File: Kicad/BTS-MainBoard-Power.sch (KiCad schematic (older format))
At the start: 46 parts, among them J1 +12VIn, J10 Conn_01x02, J11 Conn_01x02, J12 Conn_01x02, J13 Conn_01x02, J14 Conn_01x02, J15 Conn_01x02, J16 Conn_01x02, J17 Conn_01x02, J18 Conn_01x02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

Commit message: Renamed Libraries and renamed project files as well
Signed-off-by: bebenlebricolo <benoittarrade@hotmail.fr>
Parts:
- removed U2, U3, U4, U5: STD80N6F6, Package_TO_SOT_SMD:TO-252-2, symbol STD80N6F6:STD80N6F6
- added Q1, Q2, Q3, Q4: STD80N6F6, Package_TO_SOT_SMD:TO-252-2, symbol Device:Q_NMOS_GDS
- J1, J2: footprint PeltierSwitchingMainBoard:Power_Solder_Pad_7x15mm -> BTS-MainBoard-Power:Power_Solder_Pad_7x15mm
- J10, J11, J4, J5, J6, J7, J8, J9: footprint PeltierSwitchingMainBoard:Power_Solder_Pad_5x10mm_02 -> BTS-MainBoard-Power:Power_Solder_Pad_5x10mm_02
- L1, L2, L3, L4: footprint PeltierSwitchingMainBoard:L_Bourns_SRP1270 -> BTS-MainBoard-Power:L_Bourns_SRP1270
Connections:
- net +12V: now also Q1.2 (D), Q3.2 (D)
- net AHS: now also Q1.3 (S), Q2.2 (D)
- net ALS: now also Q2.3 (S), Q4.3 (S)
- net BHS: now also Q3.3 (S), Q4.2 (D)
- net at R8.1: now also Q2.1 (G)
- net at R7.1: now also Q1.1 (G)
- net at R10.1: now also Q3.1 (G)
- net at R11.1: now also Q4.1 (G)
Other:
- moved on the sheet: R10, R11, R7, R8
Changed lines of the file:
@@
 $EndDescr
-$Comp
-L STD80N6F6:STD80N6F6 U3
-U 1 1 6138C674
-P 5900 3900
-F 0 "U3" H 6330 4053 60  0000 L CNN
-F 1 "STD80N6F6" H 6330 3947 60  0000 L CNN
-F 2 "Package_TO_SOT_SMD:TO-252-2" H 6350 3740 60  0001 C CNN
-F 3 "" H 5900 3900 60  0000 C CNN
-	1    5900 3900
-	1    0    0    -1
-$EndComp
 $Comp
 L power:+12V #PWR01
@@
 L Device:R R7
 U 1 1 613B719E
-P 5750 2650
-F 0 "R7" V 5543 2650 50  0000 C CNN
-F 1 "3.3" V 5634 2650 50  0000 C CNN
-F 2 "Resistor_SMD:R_1206_3216Metric_Pad1.30x1.75mm_HandSolder" V 5680 2650 50  0001 C CNN
-F 3 "~" H 5750 2650 50  0001 C CNN
-	1    5750 2650
+P 5750 2600
+F 0 "R7" V 5543 2600 50  0000 C CNN
+F 1 "3.3" V 5634 2600 50  0000 C CNN
+F 2 "Resistor_SMD:R_1206_3216Metric_Pad1.30x1.75mm_HandSolder" V 5680 2600 50  0001 C CNN
+F 3 "~" H 5750 2600 50  0001 C CNN
+	1    5750 2600
 	0    1    1    0
 $EndComp
@@
 L Device:R R8
 U 1 1 613BA065
-P 5750 3900
-F 0 "R8" V 5543 3900 50  0000 C CNN
-F 1 "3.3" V 5634 3900 50  0000 C CNN
-F 2 "Resistor_SMD:R_1206_3216Metric_Pad1.30x1.75mm_HandSolder" V 5680 3900 50  0001 C CNN
-F 3 "~" H 5750 3900 50  0001 C CNN
-	1    5750 3900
+P 5750 3850
+F 0 "R8" V 5543 3850 50  0000 C CNN
+F 1 "3.3" V 5634 3850 50  0000 C CNN
+F 2 "Resistor_SMD:R_1206_3216Metric_Pad1.30x1.75mm_HandSolder" V 5680 3850 50  0001 C CNN
+F 3 "~" H 5750 3850 50  0001 C CNN
+	1    5750 3850
 	0    1    1    0
 $EndComp
@@
 L Device:R R10
 U 1 1 613C9CA0
-P 7250 2650
-F 0 "R10" V 7043 2650 50  0000 C CNN
-F 1 "3.3" V 7134 2650 50  0000 C CNN
-F 2 "Resistor_SMD:R_1206_3216Metric_Pad1.30x1.75mm_HandSolder" V 7180 2650 50  0001 C CNN
-F 3 "~" H 7250 2650 50  0001 C CNN
-	1    7250 2650
+P 7250 2600
+F 0 "R10" V 7043 2600 50  0000 C CNN
+F 1 "3.3" V 7134 2600 50  0000 C CNN
+F 2 "Resistor_SMD:R_1206_3216Metric_Pad1.30x1.75mm_HandSolder" V 7180 2600 50  0001 C CNN
+F 3 "~" H 7250 2600 50  0001 C CNN
+	1    7250 2600
 	0    1    1    0
 $EndComp
@@
 L Device:R R11
 U 1 1 613CB9E6
-P 7250 3900
-F 0 "R11" V 7043 3900 50  0000 C CNN
-F 1 "3.3" V 7134 3900 50  0000 C CNN
-F 2 "Resistor_SMD:R_1206_3216Metric_Pad1.30x1.75mm_HandSolder" V 7180 3900 50  0001 C CNN
-F 3 "~" H 7250 3900 50  0001 C CNN
-	1    7250 3900
+P 7250 3850
+F 0 "R11" V 7043 3850 50  0000 C CNN
+F 1 "3.3" V 7134 3850 50  0000 C CNN
+F 2 "Resistor_SMD:R_1206_3216Metric_Pad1.30x1.75mm_HandSolder" V 7180 3850 50  0001 C CNN
+F 3 "~" H 7250 3850 50  0001 C CNN
+	1    7250 3850
 	0    1    1    0
 $EndComp
@@
 Wire Wire Line
 	6950 4500 7700 4500
-$Comp
-L STD80N6F6:STD80N6F6 U2
-U 1 1 613DD883
-P 5900 2650
-F 0 "U2" H 6330 2803 60  0000 L CNN
-F 1 "STD80N6F6" H 6330 2697 60  0000 L CNN
-F 2 "Package_TO_SOT_SMD:TO-252-2" H 6350 2490 60  0001 C CNN
-F 3 "" H 5900 2650 60  0000 C CNN
-	1    5900 2650
-	1    0    0    -1
-$EndComp
-$Comp
-L STD80N6F6:STD80N6F6 U5
-U 1 1 613DED8D
-P 7400 3900
-F 0 "U5" H 7830 4053 60  0000 L CNN
-F 1 "STD80N6F6" H 7830 3947 60  0000 L CNN
-F 2 "Package_TO_SOT_SMD:TO-252-2" H 7850 3740 60  0001 C CNN
-F 3 "" H 7400 3900 60  0000 C CNN
-	1    7400 3900
-	1    0    0    -1
-$EndComp
-Text Label 5600 3900 2    50   ~ 0
+Text Label 5600 3850 2    50   ~ 0
 ALO
-Text Label 7100 2650 2    50   ~ 0
+Text Label 7100 2600 2    50   ~ 0
 BHO
-Text Label 7100 3900 2    50   ~ 0
+Text Label 7100 3850 2    50   ~ 0
 BLO
 Wire Wire Line
@@
 F 0 "L3" V 6790 3400 50  0000 C CNN
 F 1 "SRP1270-100M" V 6699 3400 50  0000 C CNN
-F 2 "PeltierSwitchingMainBoard:L_Bourns_SRP1270" H 6600 3400 50  0001 C CNN
+F 2 "BTS-MainBoard-Power:L_Bourns_SRP1270" H 6600 3400 50  0001 C CNN
 F 3 "~" H 6600 3400 50  0001 C CNN
 	1    6600 3400
@@
 F 0 "L4" V 6790 3650 50  0000 C CNN
 F 1 "SRP1270-100M" V 6699 3650 50  0000 C CNN
-F 2 "PeltierSwitchingMainBoard:L_Bourns_SRP1270" H 6600 3650 50  0001 C CNN
+F 2 "BTS-MainBoard-Power:L_Bourns_SRP1270" H 6600 3650 50  0001 C CNN
 F 3 "~" H 6600 3650 50  0001 C CNN
 	1    6600 3650
@@
 F 0 "L1" V 6790 2900 50  0000 C CNN
 F 1 "SRP1270-100M" V 6699 2900 50  0000 C CNN
-F 2 "PeltierSwitchingMainBoard:L_Bourns_SRP1270" H 6600 2900 50  0001 C CNN
+F 2 "BTS-MainBoard-Power:L_Bourns_SRP1270" H 6600 2900 50  0001 C CNN
 F 3 "~" H 6600 2900 50  0001 C CNN
 	1    6600 2900
@@
 F 0 "L2" V 6790 3200 50  0000 C CNN
 F 1 "SRP1270-100M" V 6699 3200 50  0000 C CNN
-F 2 "PeltierSwitchingMainBoard:L_Bourns_SRP1270" H 6600 3200 50  0001 C CNN
+F 2 "BTS-MainBoard-Power:L_Bourns_SRP1270" H 6600 3200 50  0001 C CNN
 F 3 "~" H 6600 3200 50  0001 C CNN
 	1    6600 3200
@@
 Wire Wire Line
 	7700 2800 7700 2950
-Wire Wire Line
-	7700 1650 7700 2300
-$Comp
-L STD80N6F6:STD80N6F6 U4
-U 1 1 613DE25E
-P 7400 2650
-F 0 "U4" H 7830 2803 60  0000 L CNN
-F 1 "STD80N6F6" H 7830 2697 60  0000 L CNN
-F 2 "Package_TO_SOT_SMD:TO-252-2" H 7850 2490 60  0001 C CNN
-F 3 "" H 7400 2650 60  0000 C CNN
-	1    7400 2650
-	1    0    0    -1
-$EndComp
-Wire Wire Line
-	6200 2300 6200 1650
-Wire Wire Line
-	7700 3550 7700 3200
 Connection ~ 7700 3200
 Wire Wire Line
@@
 	6200 4050 6200 4300
 Connection ~ 6200 4300
-Wire Wire Line
-	6200 3550 6200 3250
 Connection ~ 6200 3250
 $Comp
@@
 F 0 "J1" H 4330 1142 50  0000 L CNN
 F 1 "+12VIn" H 4330 1051 50  0000 L CNN
-F 2 "PeltierSwitchingMainBoard:Power_Solder_Pad_7x15mm" H 4250 1100 50  0001 C CNN
+F 2 "BTS-MainBoard-Power:Power_Solder_Pad_7x15mm" H 4250 1100 50  0001 C CNN
 F 3 "~" H 4250 1100 50  0001 C CNN
 	1    4250 1100
@@
 F 0 "J2" H 4330 1342 50  0000 L CNN
 F 1 "GNDIn" H 4330 1251 50  0000 L CNN
-F 2 "PeltierSwitchingMainBoard:Power_Solder_Pad_7x15mm" H 4250 1300 50  0001 C CNN
+F 2 "BTS-MainBoard-Power:Power_Solder_Pad_7x15mm" H 4250 1300 50  0001 C CNN
 F 3 "~" H 4250 1300 50  0001 C CNN
 	1    4250 1300
@@
 F 0 "J4" H 10130 1092 50  0000 L CNN
 F 1 "Conn_01x02" H 10130 1001 50  0000 L CNN
-F 2 "PeltierSwitchingMainBoard:Power_Solder_Pad_5x10mm_02" H 10050 1100 50  0001 C CNN
+F 2 "BTS-MainBoard-Power:Power_Solder_Pad_5x10mm_02" H 10050 1100 50  0001 C CNN
 F 3 "~" H 10050 1100 50  0001 C CNN
 	1    10050 1100
@@
 F 0 "J5" H 10130 1342 50  0000 L CNN
 F 1 "Conn_01x02" H 10130 1251 50  0000 L CNN
-F 2 "PeltierSwitchingMainBoard:Power_Solder_Pad_5x10mm_02" H 10050 1350 50  0001 C CNN
+F 2 "BTS-MainBoard-Power:Power_Solder_Pad_5x10mm_02" H 10050 1350 50  0001 C CNN
 F 3 "~" H 10050 1350 50  0001 C CNN
 	1    10050 1350
@@
 F 0 "J6" H 10130 1592 50  0000 L CNN
 F 1 "Conn_01x02" H 10130 1501 50  0000 L CNN
-F 2 "PeltierSwitchingMainBoard:Power_Solder_Pad_5x10mm_02" H 10050 1600 50  0001 C CNN
+F 2 "BTS-MainBoard-Power:Power_Solder_Pad_5x10mm_02" H 10050 1600 50  0001 C CNN
 F 3 "~" H 10050 1600 50  0001 C CNN
 	1    10050 1600
@@
 F 0 "J7" H 10130 1842 50  0000 L CNN
 F 1 "Conn_01x02" H 10130 1751 50  0000 L CNN
-F 2 "PeltierSwitchingMainBoard:Power_Solder_Pad_5x10mm_02" H 10050 1850 50  0001 C CNN
+F 2 "BTS-MainBoard-Power:Power_Solder_Pad_5x10mm_02" H 10050 1850 50  0001 C CNN
 F 3 "~" H 10050 1850 50  0001 C CNN
 	1    10050 1850
@@
 F 0 "J8" H 10130 2092 50  0000 L CNN
 F 1 "Conn_01x02" H 10130 2001 50  0000 L CNN
-F 2 "PeltierSwitchingMainBoard:Power_Solder_Pad_5x10mm_02" H 10050 2100 50  0001 C CNN
+F 2 "BTS-MainBoard-Power:Power_Solder_Pad_5x10mm_02" H 10050 2100 50  0001 C CNN
 F 3 "~" H 10050 2100 50  0001 C CNN
 	1    10050 2100
@@
 F 0 "J9" H 10130 2342 50  0000 L CNN
 F 1 "Conn_01x02" H 10130 2251 50  0000 L CNN
-F 2 "PeltierSwitchingMainBoard:Power_Solder_Pad_5x10mm_02" H 10050 2350 50  0001 C CNN
+F 2 "BTS-MainBoard-Power:Power_Solder_Pad_5x10mm_02" H 10050 2350 50  0001 C CNN
 F 3 "~" H 10050 2350 50  0001 C CNN
 	1    10050 2350
@@
 F 0 "J10" H 10130 2592 50  0000 L CNN
 F 1 "Conn_01x02" H 10130 2501 50  0000 L CNN
-F 2 "PeltierSwitchingMainBoard:Power_Solder_Pad_5x10mm_02" H 10050 2600 50  0001 C CNN
+F 2 "BTS-MainBoard-Power:Power_Solder_Pad_5x10mm_02" H 10050 2600 50  0001 C CNN
 F 3 "~" H 10050 2600 50  0001 C CNN
 	1    10050 2600
@@
 F 0 "J11" H 10130 2842 50  0000 L CNN
 F 1 "Conn_01x02" H 10130 2751 50  0000 L CNN
-F 2 "PeltierSwitchingMainBoard:Power_Solder_Pad_5x10mm_02" H 10050 2850 50  0001 C CNN
+F 2 "BTS-MainBoard-Power:Power_Solder_Pad_5x10mm_02" H 10050 2850 50  0001 C CNN
 F 3 "~" H 10050 2850 50  0001 C CNN
 	1    10050 2850
@@
 	0    1    1    0
 $EndComp
-Text Label 5600 2650 2    50   ~ 0
+Text Label 5600 2600 2    50   ~ 0
 AHO
 Wire Wire Line
@@
 Text Notes 9800 6450 0    50   Italic 0
 Designed by Benoit Tarrade\n(alias bebenlebricolo)\nhttps://github.com/bebenlebricolo
+$Comp
+L Device:Q_NMOS_GDS Q1
+U 1 1 6140C534
+P 6100 2600
+F 0 "Q1" H 6305 2646 50  0000 L CNN
+F 1 "STD80N6F6" H 6305 2555 50  0000 L CNN
+F 2 "Package_TO_SOT_SMD:TO-252-2" H 6300 2700 50  0001 C CNN
+F 3 "~" H 6100 2600 50  0001 C CNN
+	1    6100 2600
+	1    0    0    -1
+$EndComp
+Wire Wire Line
+	6200 3250 6200 3650
+Wire Wire Line
+	6200 1650 6200 2400
+Wire Wire Line
+	7700 3200 7700 3650
+Wire Wire Line
+	7700 1650 7700 2400
+$Comp
+L Device:Q_NMOS_GDS Q3
+U 1 1 61418DBA
+P 7600 2600
+F 0 "Q3" H 7805 2646 50  0000 L CNN
+F 1 "STD80N6F6" H 7805 2555 50  0000 L CNN
+F 2 "Package_TO_SOT_SMD:TO-252-2" H 7800 2700 50  0001 C CNN
+F 3 "~" H 7600 2600 50  0001 C CNN
+	1    7600 2600
+	1    0    0    -1
+$EndComp
+$Comp
+L Device:Q_NMOS_GDS Q4
+U 1 1 614197F7
+P 7600 3850
+F 0 "Q4" H 7805 3896 50  0000 L CNN
+F 1 "STD80N6F6" H 7805 3805 50  0000 L CNN
+F 2 "Package_TO_SOT_SMD:TO-252-2" H 7800 3950 50  0001 C CNN
+F 3 "~" H 7600 3850 50  0001 C CNN
+	1    7600 3850
+	1    0    0    -1
+$EndComp
+$Comp
+L Device:Q_NMOS_GDS Q2
+U 1 1 61419F8A
+P 6100 3850
+F 0 "Q2" H 6305 3896 50  0000 L CNN
+F 1 "STD80N6F6" H 6305 3805 50  0000 L CNN
+F 2 "Package_TO_SOT_SMD:TO-252-2" H 6300 3950 50  0001 C CNN
+F 3 "~" H 6100 3850 50  0001 C CNN
+	1    6100 3850
+	1    0    0    -1
+$EndComp
 $EndSCHEMATC

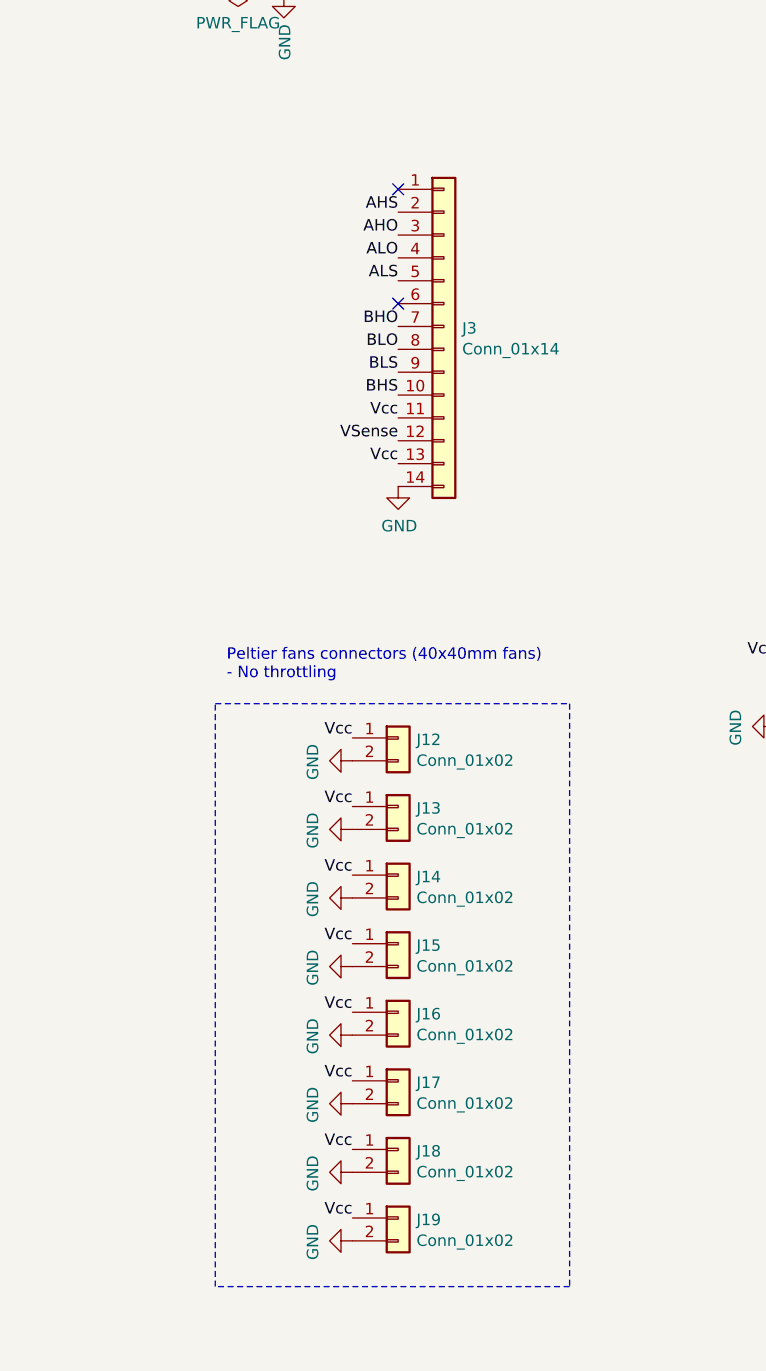
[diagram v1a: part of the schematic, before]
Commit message: Updated board with FANDRIVE power signal and silkscreen
Signed-off-by: bebenlebricolo <benoittarrade@hotmail.fr>
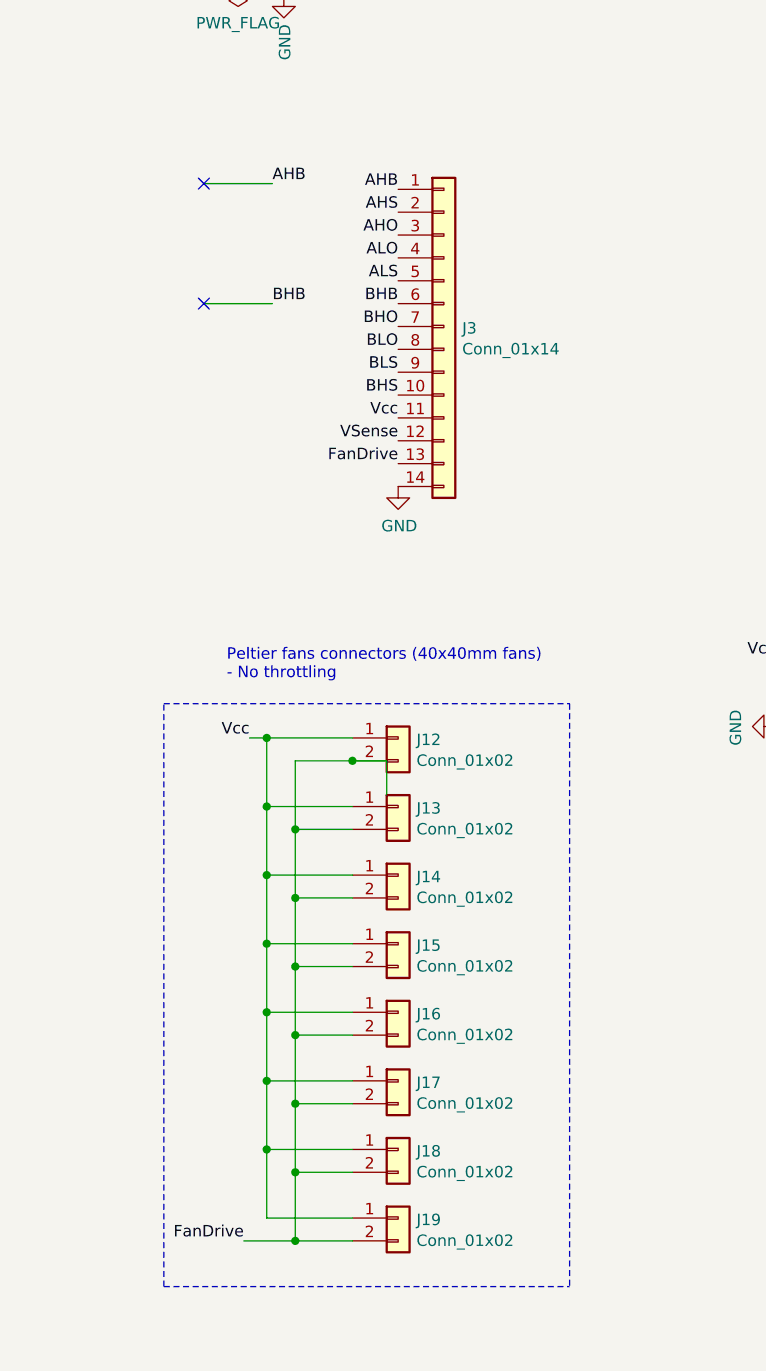
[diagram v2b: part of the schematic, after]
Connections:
- net +12V: no longer J3.13 (Pin_13)
- net GND: no longer J12.2 (Pin_2), J13.2 (Pin_2), J14.2 (Pin_2), J15.2 (Pin_2), J16.2 (Pin_2), J17.2 (Pin_2), J18.2 (Pin_2), J19.2 (Pin_2)
- net AHB: now reaches J3.1 (Pin_1)
- net BHB: now reaches J3.6 (Pin_6)
- new net FanDrive: J12.2 (Pin_2), J13.2 (Pin_2), J14.2 (Pin_2), J15.2 (Pin_2), J16.2 (Pin_2), J17.2 (Pin_2), J18.2 (Pin_2), J19.2 (Pin_2), J3.13 (Pin_13)
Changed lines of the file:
@@
 	1    0    0    -1
 $EndComp
-NoConn ~ 2650 2550
-NoConn ~ 2650 3050
 Text Label 2650 2650 2    50   ~ 0
 AHS
@@
 Wire Wire Line
 	6200 4500 6950 4500
-Text Label 2650 3750 2    50   ~ 0
-Vcc
 $Comp
 L Device:R R1
@@
 	1    0    0    -1
 $EndComp
-Text Label 2450 4950 2    50   ~ 0
-Vcc
-$Comp
-L power:GND #PWR08
-U 1 1 613B59DC
-P 2450 5050
-F 0 "#PWR08" H 2450 4800 50  0001 C CNN
-F 1 "GND" H 2455 4877 50  0000 C CNN
-F 2 "" H 2450 5050 50  0001 C CNN
-F 3 "" H 2450 5050 50  0001 C CNN
-	1    2450 5050
-	0    1    1    0
-$EndComp
 $Comp
 L Connector_Generic:Conn_01x02 J13
@@
 	1    0    0    -1
 $EndComp
-Text Label 2450 5250 2    50   ~ 0
-Vcc
-$Comp
-L power:GND #PWR09
-U 1 1 613B697D
-P 2450 5350
-F 0 "#PWR09" H 2450 5100 50  0001 C CNN
-F 1 "GND" H 2455 5177 50  0000 C CNN
-F 2 "" H 2450 5350 50  0001 C CNN
-F 3 "" H 2450 5350 50  0001 C CNN
-	1    2450 5350
-	0    1    1    0
-$EndComp
 $Comp
 L Connector_Generic:Conn_01x02 J14
@@
 	1    0    0    -1
 $EndComp
-Text Label 2450 5550 2    50   ~ 0
-Vcc
-$Comp
-L power:GND #PWR010
-U 1 1 613BB845
-P 2450 5650
-F 0 "#PWR010" H 2450 5400 50  0001 C CNN
-F 1 "GND" H 2455 5477 50  0000 C CNN
-F 2 "" H 2450 5650 50  0001 C CNN
-F 3 "" H 2450 5650 50  0001 C CNN
-	1    2450 5650
-	0    1    1    0
-$EndComp
 $Comp
 L Connector_Generic:Conn_01x02 J15
@@
 	1    0    0    -1
 $EndComp
-Text Label 2450 5850 2    50   ~ 0
-Vcc
-$Comp
-L power:GND #PWR019
-U 1 1 613BCBA4
-P 2450 5950
-F 0 "#PWR019" H 2450 5700 50  0001 C CNN
-F 1 "GND" H 2455 5777 50  0000 C CNN
-F 2 "" H 2450 5950 50  0001 C CNN
-F 3 "" H 2450 5950 50  0001 C CNN
-	1    2450 5950
-	0    1    1    0
-$EndComp
 $Comp
 L Connector_Generic:Conn_01x02 J16
@@
 	1    0    0    -1
 $EndComp
-Text Label 2450 6150 2    50   ~ 0
-Vcc
-$Comp
-L power:GND #PWR020
-U 1 1 613BE04D
-P 2450 6250
-F 0 "#PWR020" H 2450 6000 50  0001 C CNN
-F 1 "GND" H 2455 6077 50  0000 C CNN
-F 2 "" H 2450 6250 50  0001 C CNN
-F 3 "" H 2450 6250 50  0001 C CNN
-	1    2450 6250
-	0    1    1    0
-$EndComp
 $Comp
 L Connector_Generic:Conn_01x02 J17
@@
 	1    0    0    -1
 $EndComp
-Text Label 2450 6450 2    50   ~ 0
-Vcc
-$Comp
-L power:GND #PWR021
-U 1 1 613BF42D
-P 2450 6550
-F 0 "#PWR021" H 2450 6300 50  0001 C CNN
-F 1 "GND" H 2455 6377 50  0000 C CNN
-F 2 "" H 2450 6550 50  0001 C CNN
-F 3 "" H 2450 6550 50  0001 C CNN
-	1    2450 6550
-	0    1    1    0
-$EndComp
 $Comp
 L Connector_Generic:Conn_01x02 J18
@@
 	1    0    0    -1
 $EndComp
-Text Label 2450 6750 2    50   ~ 0
-Vcc
-$Comp
-L power:GND #PWR022
-U 1 1 613C08FF
-P 2450 6850
-F 0 "#PWR022" H 2450 6600 50  0001 C CNN
-F 1 "GND" H 2455 6677 50  0000 C CNN
-F 2 "" H 2450 6850 50  0001 C CNN
-F 3 "" H 2450 6850 50  0001 C CNN
-	1    2450 6850
-	0    1    1    0
-$EndComp
 $Comp
 L Connector_Generic:Conn_01x02 J19
@@
 	1    0    0    -1
 $EndComp
-Text Label 2450 7050 2    50   ~ 0
-Vcc
-$Comp
-L power:GND #PWR023
-U 1 1 613C1D1E
-P 2450 7150
-F 0 "#PWR023" H 2450 6900 50  0001 C CNN
-F 1 "GND" H 2455 6977 50  0000 C CNN
-F 2 "" H 2450 7150 50  0001 C CNN
-F 3 "" H 2450 7150 50  0001 C CNN
-	1    2450 7150
-	0    1    1    0
-$EndComp
 Wire Notes Line
-	1850 4800 3400 4800
-Wire Notes Line
-	3400 4800 3400 7350
-Wire Notes Line
-	3400 7350 1850 7350
-Wire Notes Line
-	1850 7350 1850 4800
+	1625 7350 1625 4800
 Text Notes 1900 4700 0    50   ~ 0
 Peltier fans connectors (40x40mm fans)\n- No throttling
@@
 	1    0    0    -1
 $EndComp
+Text Label 2650 3750 2    50   ~ 0
+FanDrive
+Wire Wire Line
+	2075 7050 2450 7050
+Wire Wire Line
+	2450 6750 2075 6750
+Connection ~ 2075 6750
+Wire Wire Line
+	2075 6750 2075 7050
+Wire Wire Line
+	2450 6450 2075 6450
+Connection ~ 2075 6450
+Wire Wire Line
+	2075 6450 2075 6750
+Wire Wire Line
+	2450 6150 2075 6150
+Connection ~ 2075 6150
+Wire Wire Line
+	2075 6150 2075 6450
+Wire Wire Line
+	2450 5850 2075 5850
+Connection ~ 2075 5850
+Wire Wire Line
+	2075 5850 2075 6150
+Wire Wire Line
+	2450 5550 2075 5550
+Connection ~ 2075 5550
+Wire Wire Line
+	2075 5550 2075 5850
+Wire Wire Line
+	2450 5250 2075 5250
+Connection ~ 2075 5250
+Wire Wire Line
+	2075 5250 2075 5550
+Wire Wire Line
+	2450 4950 2075 4950
+Connection ~ 2075 4950
+Wire Wire Line
+	2075 4950 2075 5250
+Wire Wire Line
+	2600 5200 2600 5050
+Wire Wire Line
+	2600 5050 2450 5050
+Wire Wire Line
+	2450 5050 2200 5050
+Wire Wire Line
+	2200 7150 2450 7150
+Connection ~ 2450 5050
+Wire Wire Line
+	2450 6850 2200 6850
+Connection ~ 2200 6850
+Wire Wire Line
+	2200 6850 2200 7150
+Wire Wire Line
+	2450 6550 2200 6550
+Connection ~ 2200 6550
+Wire Wire Line
+	2200 6550 2200 6850
+Wire Wire Line
+	2450 6250 2200 6250
+Connection ~ 2200 6250
+Wire Wire Line
+	2200 6250 2200 6550
+Wire Wire Line
+	2450 5950 2200 5950
+Connection ~ 2200 5950
+Wire Wire Line
+	2200 5950 2200 6250
+Wire Wire Line
+	2450 5650 2200 5650
+Wire Wire Line
+	2200 5050 2200 5350
+Connection ~ 2200 5650
+Wire Wire Line
+	2200 5650 2200 5950
+Wire Wire Line
+	2450 5350 2200 5350
+Connection ~ 2200 5350
+Wire Wire Line
+	2200 5350 2200 5650
+Text Label 1975 7150 2    50   ~ 0
+FanDrive
+Text Label 2000 4950 2    50   ~ 0
+Vcc
+Wire Wire Line
+	2075 4950 2000 4950
+Wire Notes Line
+	1625 4800 3400 4800
+Wire Notes Line
+	1625 7350 3400 7350
+Wire Notes Line
+	3400 4800 3400 7350
+Wire Wire Line
+	1975 7150 2200 7150
+Connection ~ 2200 7150
+Text Label 2650 2550 2    50   ~ 0
+AHB
+Text Label 2650 3050 2    50   ~ 0
+BHB
+Text Label 2100 2525 0    50   ~ 0
+AHB
+Wire Wire Line
+	2100 2525 1800 2525
+Wire Wire Line
+	2100 3050 1800 3050
+Text Label 2100 3050 0    50   ~ 0
+BHB
+NoConn ~ 1800 2525
+NoConn ~ 1800 3050
 $EndSCHEMATC
